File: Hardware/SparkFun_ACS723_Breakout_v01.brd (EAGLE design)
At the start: 24.1 x 15.2 mm, 13 parts, among them U1 ACS712

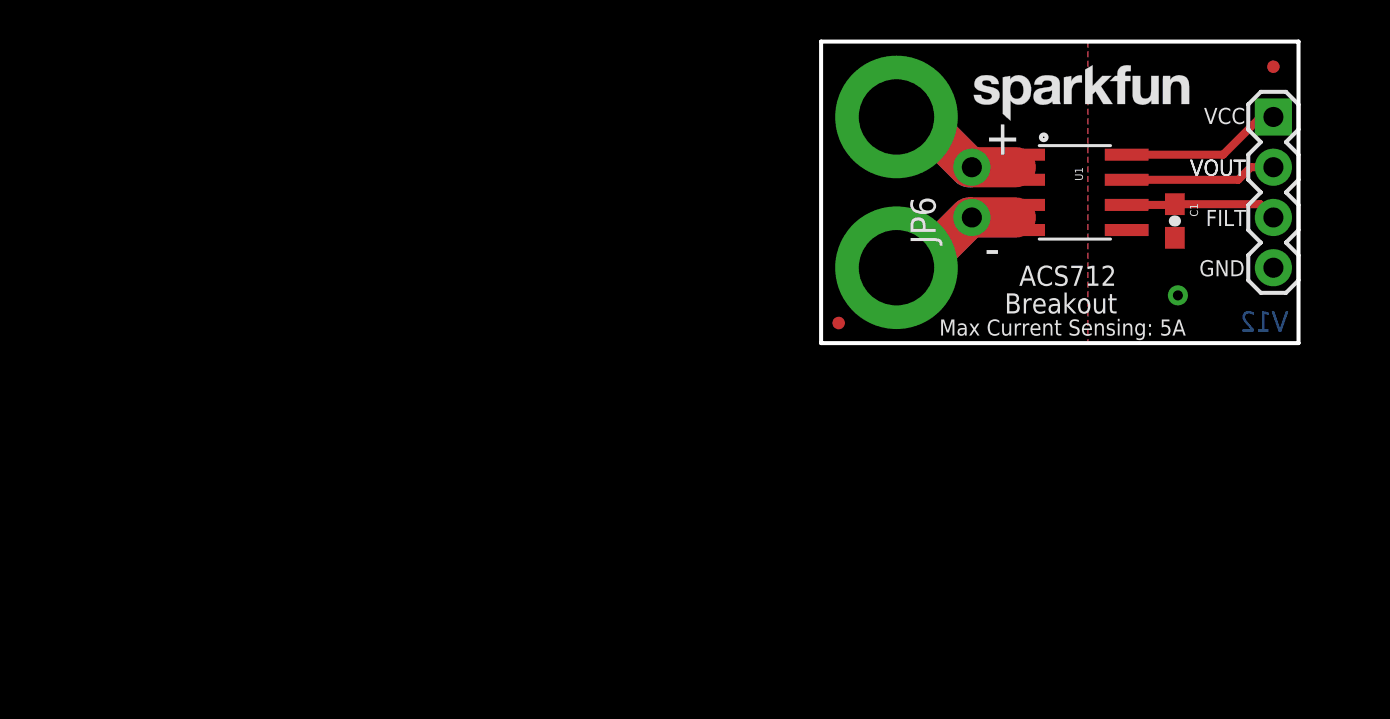
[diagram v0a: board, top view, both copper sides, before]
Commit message: removed old design and started new design
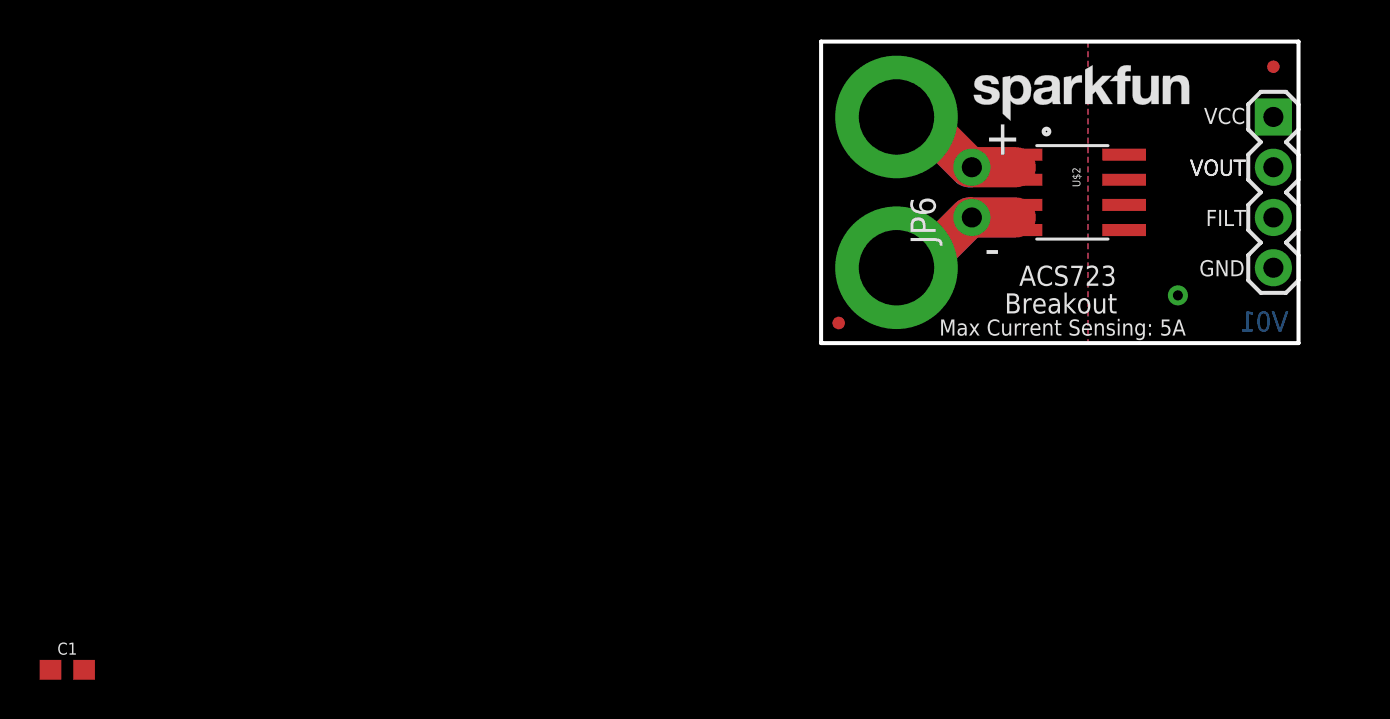
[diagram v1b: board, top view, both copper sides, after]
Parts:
- removed U1: ACS712, SparkFun-AnalogIC:SO08
- added U$2: ACS723, SparkFun-IC-Power:SO08
- C1: value 1nF -> 0.1uF; device SparkFun-Capacitors:0603-CAP -> SparkFun-Capacitors:0603
- moved C1 60.4 mm to (-40.6, -16.5), turned to 0 degrees
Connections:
- removed net FILT: C1.1, JP3.3, U1.6
- removed net GND: C1.2, JP3.4, U1.5
- removed net VOUT: JP3.2, U1.7
- new net N$1: C1.2
- net IP+: now also U$2.1, U$2.2; no longer U1.1, U1.2
- net IP-: now also U$2.3, U$2.4; no longer U1.3, U1.4
- net VCC: now also C1.1; no longer U1.8
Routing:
- net VCC: track 8.21 -> 0.00 mm
- net VOUT: track 7.76 -> 0.00 mm
- net FILT: track 7.71 -> 0.00 mm
- net IP-: track 13.4 -> 12.9 mm
- net IP+: track 13.5 -> 13.0 mm
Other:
- board text added: "ACS723"
- board text added: "Eric Orosel"
- board text added: "V01"
- board text removed: "ACS712"
- board text removed: "P. Alberts, Toni Klopfenstein"
- board text removed: "V12"

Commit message: Finalizing v01 hardware
-Adjusted silk
-Isolated high current side of the board
-added recommended filter caps
-added band-width select jumper
-changed version number
-changed chip package to ACS723
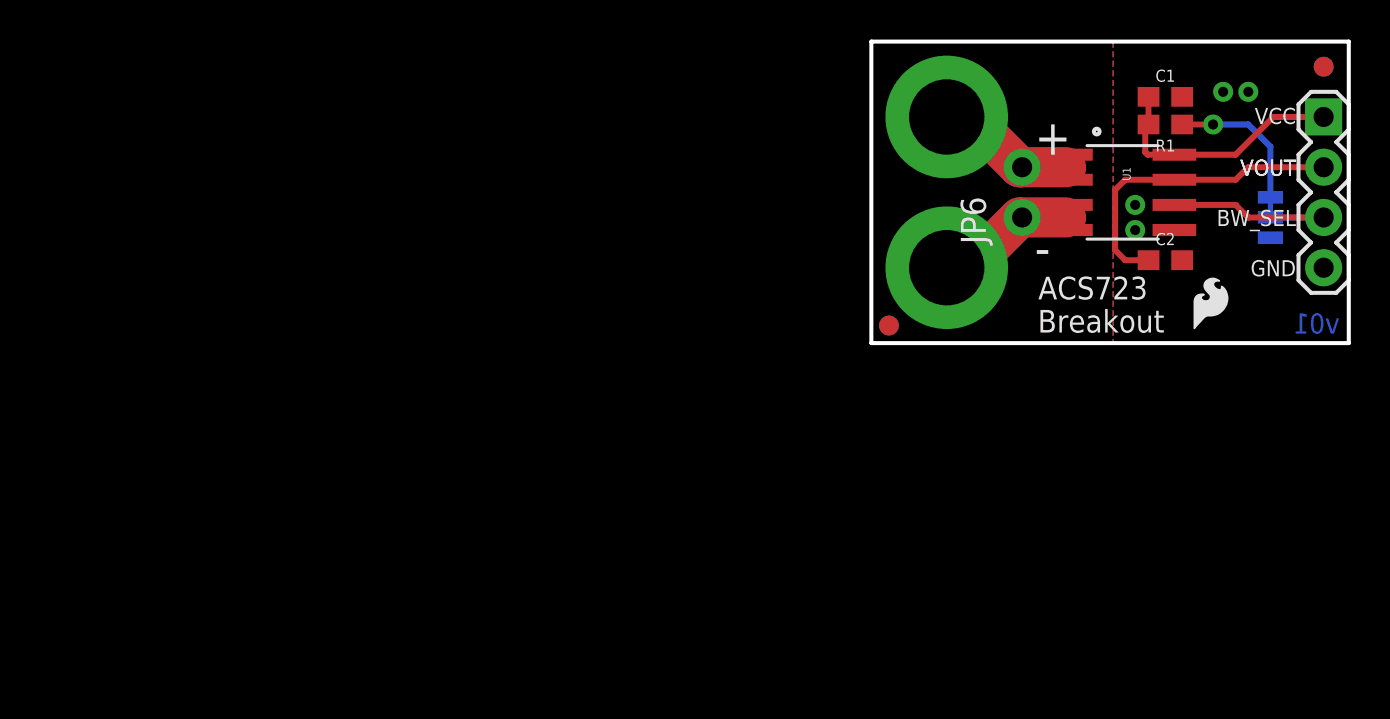
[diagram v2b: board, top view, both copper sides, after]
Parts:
- removed JP5: FIDUCIALUFIDUCIAL, SparkFun-Aesthetics:MICRO-FIDUCIAL
- removed LOGO1: SFE_LOGO_NAME.1_INCH, SparkFun-Aesthetics:SFE_LOGO_NAME_.1
- removed U$2: ACS723, SparkFun-IC-Power:SO08
- added C2: 1nF, SparkFun-Capacitors:0603
- added FD2, FD3, FD4, FD5: FIDUCIAL1X2, SparkFun-Aesthetics:FIDUCIAL-1X2
- added R1: 4.7k, SparkFun-Resistors:0603
- added U$5, U$6: (no value), SparkFun-Aesthetics:SFE_LOGO_FLAME_.1
- added U1: ACS723, SparkFun-IC-Power:SO08
- JP4: value FIDUCIALUFIDUCIAL -> JUMPER-SMT_3_1-NC_TRACE_SILK; device SparkFun-Aesthetics:MICRO-FIDUCIAL -> SparkFun-Jumpers:SMT-JUMPER_3_1-NC_TRACE_SILK
- JP6: device SparkFun-Connectors:1X02_NO_SILK -> SparkFun-Connectors:1X02_NO_SILK@1
- LOGO2: value SFE_LOGO_FLAME.3_INCH -> SFE_LOGO_NAME.1_INCH; device SparkFun-Aesthetics:SFE_LOGO_FLAME_.3 -> SparkFun-Aesthetics:SFE_LOGO_NAME_.1
- U$3: value OSHW-LOGOS -> (none); device SparkFun:OSHW-LOGO-S -> SparkFun-Aesthetics:OSHW-LOGO-M
- moved C1 62.6 mm to (14.9, 12.4)
- moved JP4 7.62 mm to (20.2, 6.35), flipped to the bottom, turned to 90 degrees
- moved LOGO2 7.02 mm to (18.8, -0.05)
- moved U$3 6.82 mm to (12.1, 8.89)
- moved FRAME1 6.48 mm to (-16.5, -11.4)
- moved U$1 6.48 mm to (-5.08, -14.0)
- moved JP1 2.54 mm to (3.81, 11.4)
- moved JP2 2.54 mm to (3.81, 3.81)
- moved JP6 2.54 mm to (7.62, 6.35)
- moved JP3 2.54 mm to (22.9, 11.4)
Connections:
- new net BW_SEL: JP3.3, JP4.2, U1.6
- new net GND: C1.2, C2.2, JP3.4, JP4.1, U1.5
- new net N$3: JP4.3, R1.1
- net IP+: now also U1.1, U1.2; no longer U$2.1, U$2.2
- net IP-: now also U1.3, U1.4; no longer U$2.3, U$2.4
- net N$1: now also C2.1, JP3.2, U1.7; no longer C1.2
- net VCC: now also R1.2, U1.8
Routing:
- net N$1: track 0.00 -> 16.0 mm
- net VCC: track 0.00 -> 12.7 mm
- net BW_SEL: track 0.00 -> 10.5 mm
- net N$3: track 0.00 -> 7.49 mm, vias 0 -> 1
- net IP-: track 12.9 -> 13.5 mm
- net IP+: track 13.0 -> 13.6 mm
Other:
- board text added: "20kHz"
- board text added: "80kHz"
- board text added: "BW_SEL"
- board text added: "v01"
- board text removed: "FILT"
- board text removed: "V01"
